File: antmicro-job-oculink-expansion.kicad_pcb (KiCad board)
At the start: 4 copper layers, 20 x 60 mm, 9 parts, among them J1 OCuLink_x4_Amphenol_G14A42121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, J2 Plug_Samtec_ERM8_2x40_ERM8-04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

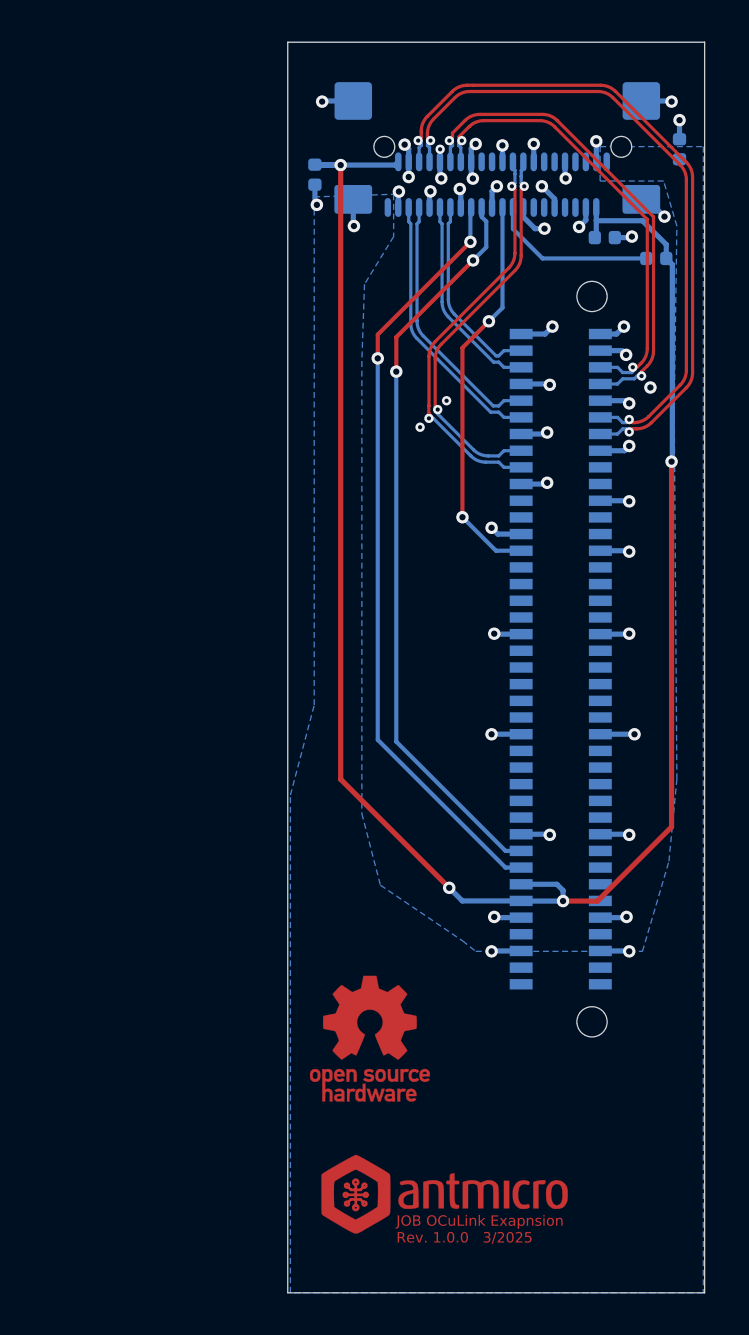
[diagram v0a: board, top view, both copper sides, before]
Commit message: [#74340] Rename project
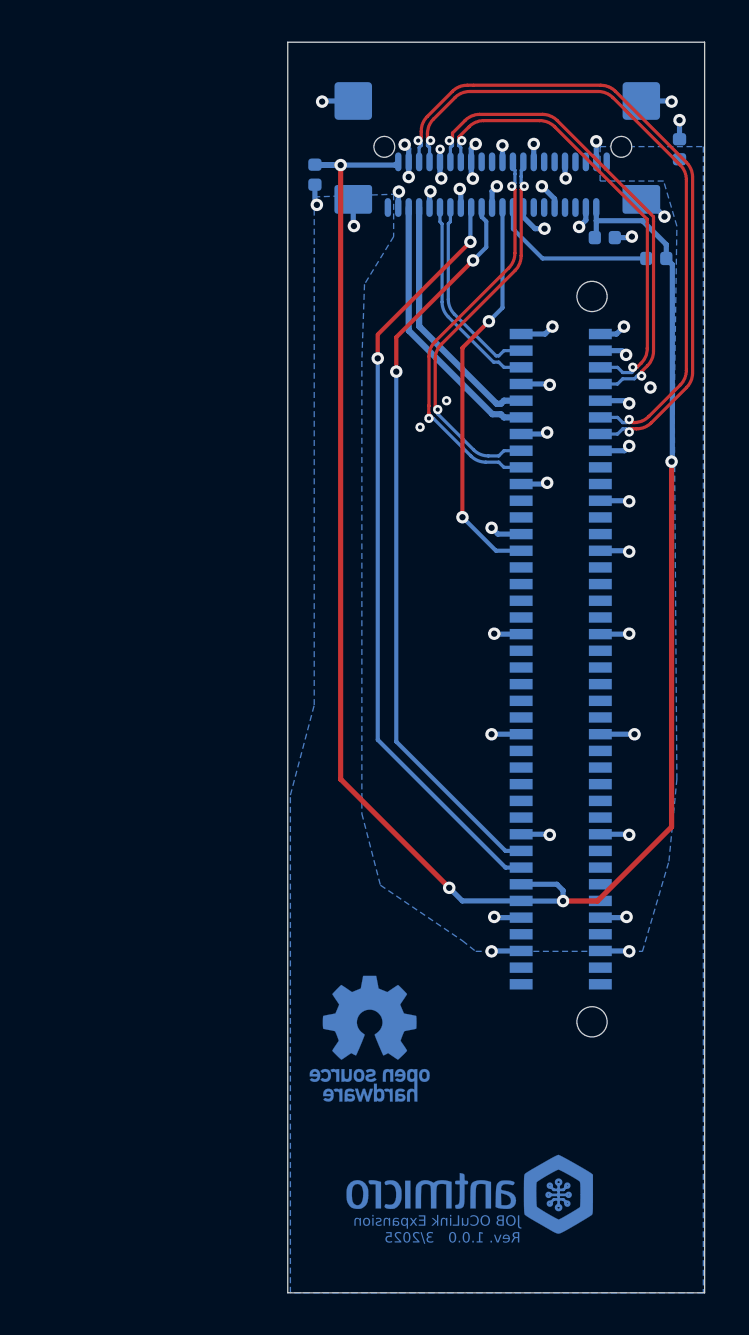
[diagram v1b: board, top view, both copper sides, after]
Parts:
- REF** (x3): moved to B.Cu
- moved REF** 1.27 mm to (202.8, 109.3), turned to 180 degrees
- turned REF** to 180 degrees (x2)
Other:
- board text added: "JOB OCuLink Expansion Rev. ${REVISION} 3/2025"
- board text removed: "JOB OCuLink Exapnsion Rev. ${REVISION} 3/2025"

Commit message: [#74340] Routing fixes
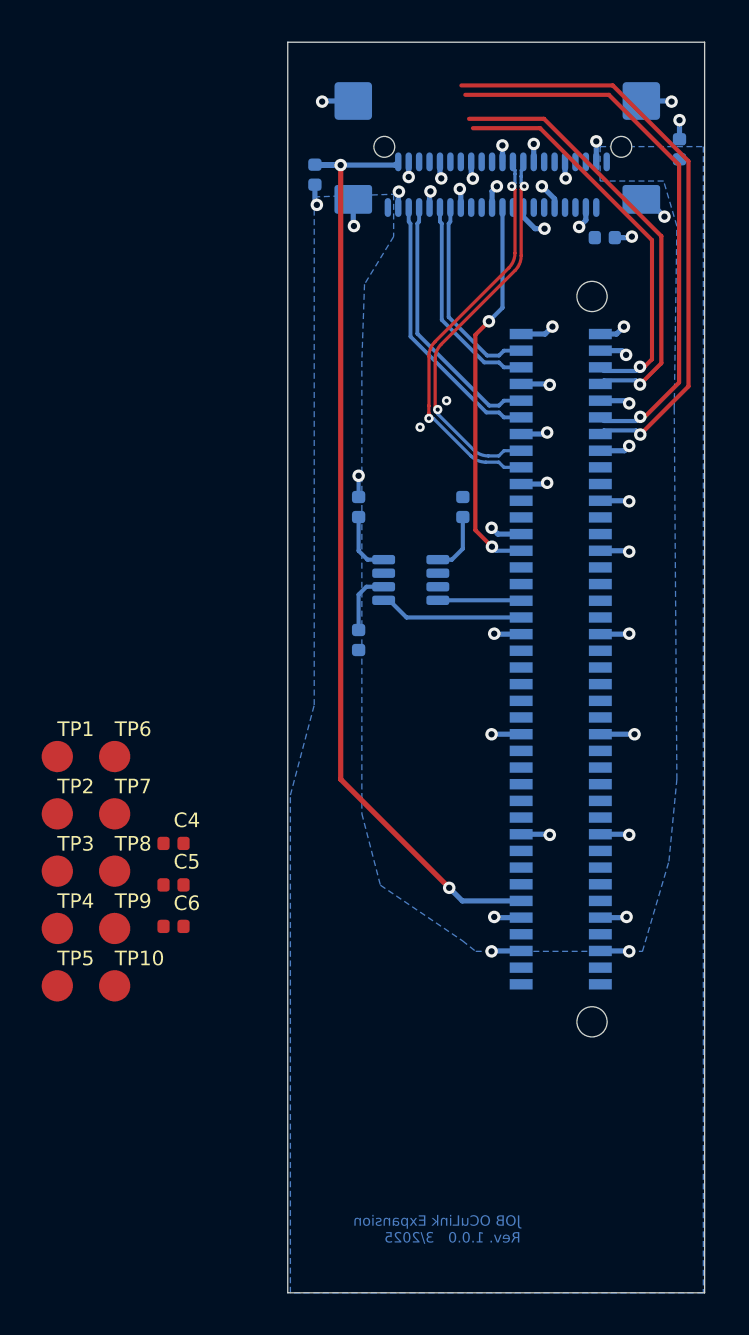
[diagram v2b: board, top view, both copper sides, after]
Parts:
- removed REF**: OSHW-Logo_5.7x6mm_Mask, antmicro-footprints:OSHW-Logo_5.7x6mm_Mask
- removed REF**: OSHW-Logo_5.7x6mm_Copper, antmicro-footprints:OSHW-Logo_5.7x6mm_Copper
- removed REF**: LOGO, antmicro-footprints:antmicro-logo_scaled_12mm
- added C4: C_10u_0402, antmicro-footprints:C_0402_1005Metric, F.Cu at (188.5, 92.4)
- added C5: C_100n_0402, antmicro-footprints:C_0402_1005Metric, F.Cu at (188.5, 94.4)
- added C6: C_100n_0402, antmicro-footprints:C_0402_1005Metric, F.Cu at (188.5, 96.4)
- added R2: R_0R_0402, antmicro-footprints:R_0402_1005Metric, B.Cu at (202.4, 76.3)
- added R3: R_10k_0402, antmicro-footprints:R_0402_1005Metric, B.Cu at (197.4, 82.7)
- added TP1: TP_1.5mm_SMD, antmicro-footprints:TP_SMD_1.5mm, F.Cu at (182.9, 88.3)
- added TP10: TP_1.5mm_SMD, antmicro-footprints:TP_SMD_1.5mm, F.Cu at (185.7, 99.3)
- added TP2: TP_1.5mm_SMD, antmicro-footprints:TP_SMD_1.5mm, F.Cu at (182.9, 91.0)
- added TP3: TP_1.5mm_SMD, antmicro-footprints:TP_SMD_1.5mm, F.Cu at (182.9, 93.8)
- added TP4: TP_1.5mm_SMD, antmicro-footprints:TP_SMD_1.5mm, F.Cu at (182.9, 96.5)
- added TP5: TP_1.5mm_SMD, antmicro-footprints:TP_SMD_1.5mm, F.Cu at (182.9, 99.3)
- added TP6: TP_1.5mm_SMD, antmicro-footprints:TP_SMD_1.5mm, F.Cu at (185.7, 88.3)
- added TP7: TP_1.5mm_SMD, antmicro-footprints:TP_SMD_1.5mm, F.Cu at (185.7, 91.0)
- added TP8: TP_1.5mm_SMD, antmicro-footprints:TP_SMD_1.5mm, F.Cu at (185.7, 93.8)
- added TP9: TP_1.5mm_SMD, antmicro-footprints:TP_SMD_1.5mm, F.Cu at (185.7, 96.5)
- added U1: MAX3373EEKA+, antmicro-footprints:SOT-23-8, B.Cu at (199.9, 79.8)
- R1: value R_10k_0402 -> R_0R_0402
- moved R1 18.6 mm to (197.4, 76.3), turned to 90 degrees
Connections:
- net /CLK+ renamed /PCIE_CLK+
- net /CLK- renamed /PCIE_CLK-
- net /PER0+ renamed /PCIE_RX0+
- net /PER0- renamed /PCIE_RX0-
- net /PER1+ renamed /PCIE_RX1+
- net /PER1- renamed /PCIE_RX1-
- net /PET0+ renamed /PCIE_TX0+
- net /PET0- renamed /PCIE_TX0-
- net /PET1+ renamed /PCIE_TX1+
- net /PET1- renamed /PCIE_TX1-
- net /SYS_SCL renamed /I2C_SCL
- net /SYS_SDA renamed /I2C_SDA
- net /~{RST} renamed /~{PCIE_RST}
- J1 pad A10: unconnected-(J1-~{CWAKE}-PadA10) -> Net-(J1-~{CWAKE})
- J2 pad 33: unconnected-(J2-Pad33) -> /JOB_GPIO07
- J2 pad 35: unconnected-(J2-Pad35) -> /JOB_GPIO09
- J2 pad 73: unconnected-(J2-Pad73) -> +1V8
- R1 pad 1: Net-(J1-~{CPRSNT}) -> /~{PCIE_CPRSNT}
- R1 pad 2: +3.3V -> Net-(J1-~{CPRSNT})
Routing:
- net +3.3V: track 90.5 -> 45.8 mm, vias 4 -> 2
- net /I2C_SCL: track 36.8 -> 0.00 mm, vias 2 -> 0
- net /I2C_SDA: track 35.7 -> 0.00 mm, vias 2 -> 0
- net Net-(J1-~{CPRSNT}): track 8.01 -> 1.02 mm, vias 0 -> 1
- net /JOB_GPIO09: track 0.00 -> 6.94 mm
- net /PCIE_RX0-: track 31.5 -> 26.7 mm, vias 2 -> 1
- net /PCIE_RX0+: track 33.0 -> 28.6 mm, vias 2 -> 1
- net /JOB_GPIO07: track 0.00 -> 4.18 mm
- net Net-(U1-~{THREE_STATE}): track 0.00 -> 3.06 mm
- net /~{PCIE_CPRSNT}: track 0.00 -> 3.00 mm
- net /~{PCIE_CWAKE}: track 0.00 -> 2.94 mm
- net /PCIE_RX1-: track 21.9 -> 19.3 mm, vias 2 -> 1
- net /PCIE_RX1+: track 23.5 -> 21.2 mm, vias 2 -> 1
- net GND: track 53.2 -> 51.3 mm, vias 48 -> 44
- net /~{PCIE_RST}: track 19.1 -> 18.6 mm

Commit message: [#74340] Finished applying fixes
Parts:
- removed TP3, TP4: TP_1.5mm_SMD, antmicro-footprints:TP_SMD_1.5mm
- added G***: LOGO, antmicro-footprints:antmicro-logo_scaled_12mm_mask, F.Cu at (205.0, 109.2)
- added REF**: OSHW-Logo_5.7x6mm_Copper, antmicro-footprints:OSHW-Logo_5.7x6mm_Copper, F.Cu at (210.0, 104.5)
- added REF**: LOGO, antmicro-footprints:antmicro-logo_scaled_12mm, F.Cu at (205.0, 109.2)
- added REF**: OSHW-Logo_5.7x6mm_Mask, antmicro-footprints:OSHW-Logo_5.7x6mm_Mask, F.Cu at (210.0, 104.5)
- C1, C2, C3, J1, J2, R1, R2, R3, U1: moved to F.Cu
- TP1, TP10, TP2, TP5, TP6, TP7, TP8, TP9: moved to B.Cu
- moved C4 35.7 mm to (209.8, 63.7), turned to 180 degrees
- moved C6 28.1 mm to (211.1, 79.6), turned to 90 degrees
- moved TP1 27.0 mm to (209.9, 88.5), turned to 180 degrees
- moved TP5 26.7 mm to (205.7, 85.3), turned to 180 degrees
- moved TP9 26.1 mm to (211.6, 99.9), turned to 180 degrees
- moved TP8 26.0 mm to (211.6, 96.1), turned to 180 degrees
- moved TP10 25.9 mm to (211.6, 98.0), turned to 180 degrees
- moved TP2 23.3 mm to (206.1, 88.5), turned to 180 degrees
- moved C5 22.6 mm to (205.6, 79.6), turned to -90 degrees
- moved TP7 21.2 mm to (201.0, 76.4), turned to 180 degrees
- moved TP6 20.6 mm to (205.7, 83.3), turned to 180 degrees
- moved C3 17.5 mm to (212.8, 60.4)
- moved C2 17.5 mm to (195.3, 59.1)
- moved R3 13.3 mm to (210.7, 82.7)
- moved C1 9.46 mm to (199.8, 63.5)
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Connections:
- U1 pad 1: /~{PCIE_CWAKE} -> /~{PCIE_CPRSNT}
- U1 pad 8: /~{PCIE_CPRSNT} -> /~{PCIE_CWAKE}
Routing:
- net +3.3V: track 45.8 -> 90.0 mm, vias 2 -> 3
- net /I2C_SCL: track 0.00 -> 38.1 mm, vias 0 -> 2
- net /I2C_SDA: track 0.00 -> 36.6 mm, vias 0 -> 2
- net +1V8: track 0.00 -> 31.2 mm, vias 0 -> 3
- net Net-(J1-~{CWAKE}): track 0.00 -> 19.3 mm, vias 0 -> 2
- net Net-(J1-~{CPRSNT}): track 1.02 -> 15.2 mm, vias 1 -> 2
- net /JOB_GPIO07: track 4.18 -> 9.18 mm, vias 0 -> 1
- net /PCIE_RX0-: track 26.7 -> 30.6 mm, vias 1 -> 2
- net /PCIE_RX0+: track 28.6 -> 32.2 mm, vias 1 -> 2
- net /~{PCIE_RST}: track 18.6 -> 22.0 mm
- net /PCIE_RX1-: track 19.3 -> 22.0 mm, vias 1 -> 2
- net /PCIE_RX1+: track 21.2 -> 23.6 mm, vias 1 -> 2
- net GND: track 51.3 -> 48.9 mm, vias 44 -> 50
- net /JOB_GPIO09: track 6.94 -> 8.61 mm, vias 0 -> 1
- net +5V: track 0.00 -> 1.51 mm, vias 0 -> 1
- added copper zone on F.Cu, net +5V
- removed copper zone on B.Cu, net +5V
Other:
- board text added: "+1.8V"
- board text added: "+3.3V"
- board text added: "+5V"
- board text added: "SCL"
- board text added: "SDA"
- board text added: "~{CPRSNT}"
- board text added: "~{CWAKE}"
- board text added: "~{RST}"

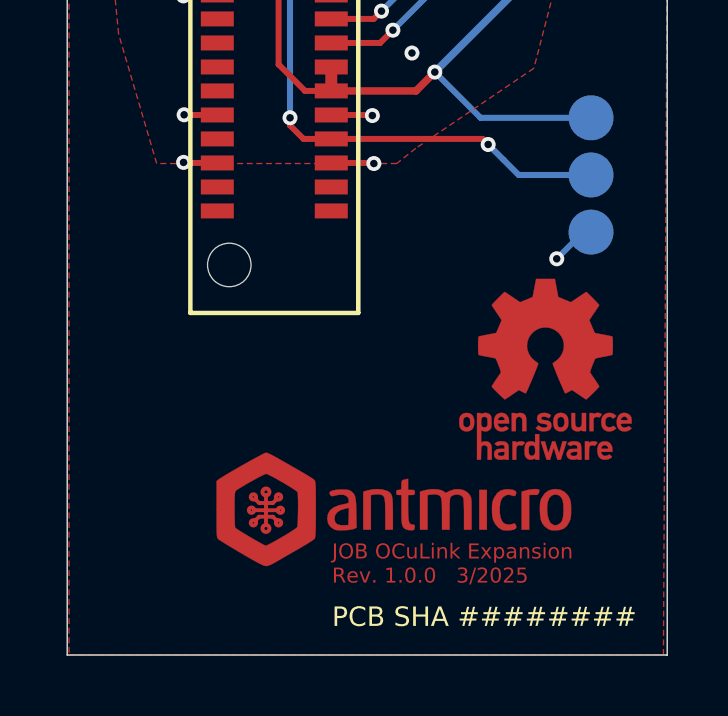
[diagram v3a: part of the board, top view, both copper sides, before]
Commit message: [#74340] Add mounting hole
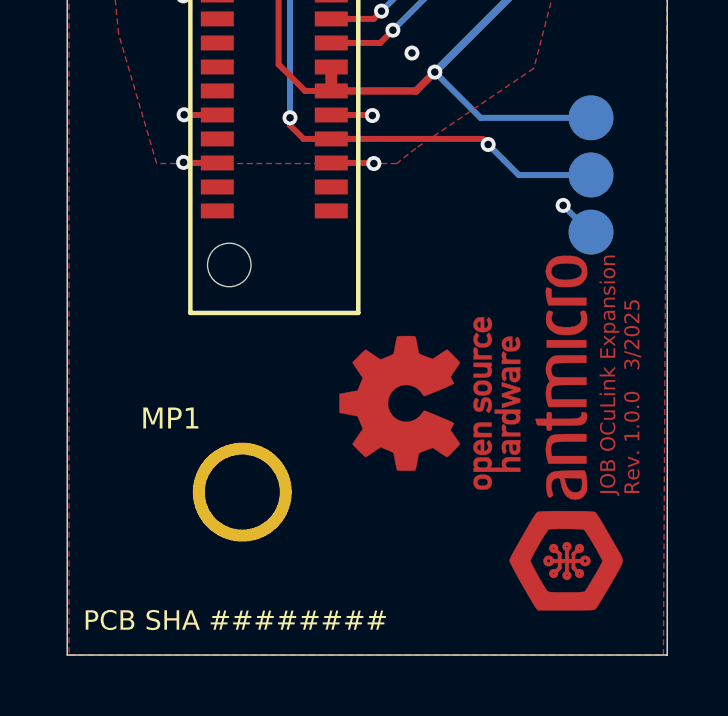
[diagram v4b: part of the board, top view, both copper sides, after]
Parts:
- added MP1: MP_Pad3.3mm_Drill2.5mm, antmicro-footprints:MP_Pad3.3mm_Drill2.5mm, F.Cu at (199.9, 108.6)
- moved G*** 6.33 mm to (210.8, 106.6), turned to 90 degrees
- moved REF** 6.33 mm to (210.8, 106.6), turned to 90 degrees
- moved REF** 4.02 mm to (206.2, 105.6), turned to 90 degrees (x2)

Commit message: [#74340] Minor cosmetic update of schematics
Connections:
- net /~{PCIE_CPRSNT} renamed /~{CPRSNT}
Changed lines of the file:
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@@
 	(net 68 "/JOB_GPIO07")
 	(net 69 "unconnected-(J2-Pad34)")
-	(net 70 "/~{PCIE_CPRSNT}")
+	(net 70 "/~{CPRSNT}")
 	(net 71 "/~{PCIE_CWAKE}")
 	(net 72 "Net-(U1-~{THREE_STATE})")
@@
 			(layers "F.Cu" "F.Paste" "F.Mask")
 			(roundrect_rratio 0.25)
-			(net 70 "/~{PCIE_CPRSNT}")
+			(net 70 "/~{CPRSNT}")
 			(pintype "passive")
 		)
@@
 			(layers "F.Cu" "F.Paste" "F.Mask")
 			(roundrect_rratio 0.25)
-			(net 70 "/~{PCIE_CPRSNT}")
+			(net 70 "/~{CPRSNT}")
 			(pinfunction "IO_V_{CC}2")
 			(pintype "bidirectional")

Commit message: [#74340] Apply Fixes
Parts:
- moved R3 0.32 mm to (210.4, 82.6)
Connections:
- net /~{CPRSNT} renamed /~{PCIE_CPRSNT}
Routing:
- net GND: track 48.9 -> 51.7 mm
- net /PCIE_RX0-: track 30.6 -> 32.4 mm
- net /PCIE_RX1-: track 22.0 -> 23.5 mm
- net +3.3V: track 90.0 -> 91.0 mm
- net /PCIE_TX1-: track 9.36 -> 9.87 mm
- net /PCIE_TX0-: track 12.5 -> 13.0 mm
